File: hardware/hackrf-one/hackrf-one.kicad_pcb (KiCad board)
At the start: 4 copper layers, 120 x 75 mm, 434 parts, among them J10 GND_CLIP, J11 Connector_USB_C_Receptacle_US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, J2 RF-SHIELD-FRAME, J3 RF-SHIELD-COVER, J4 MOUNTING_HOLE, J5 MOUNTING_HOLE, J6 MOUNTING_HOLE, J7 MOUNTING_HOLE, J8 MOUNTING_HOLE, J9 MOUNTING_HOLE, P1 1V8, P13 GPO1, P14 XCVR_CLKOUT, P15 INTR, P16 CLKIN, P17 GPO6, P18 OEB, P19 GPO3, P2 CLKOUT, P20 GPIO, P21 REF_IN, P22 I2S, P23 DBGEN, P24 TRST, P25 LPC_ISP, P26 LPC_JTAG, P27 MIXER_SDATA, P28 SD, P29 CPLD_JTAG, P3 GND, P30 BANK2_AUX, P31 MIXER_SCLK, P32 MIXER_ENX, P33 MIXER_RESETX, P34 MIX_BYPASS, P35 !MIX_BYPASS, P36 VAA, P37 SCL, P38 SDA, P39 SSP1_SCK, P4 ANTENNA, P40 SSP1_MOSI, P41 SSP1_MISO, P43 RX, P44 HP, P45 LP, P46 TX_MIX_BP, P47 RX_MIX_BP, P48 TX_AMP, P49 RX_AMP, P5 LEDS, P50 AMP_BYPASS, P51 !TX_AMP_PWR, P52 !RX_AMP_PWR, P53 CS_XCVR, P54 CS_AD, P55 TXENABLE, P56 RXENABLE, P57 XTAL2, P58 GCK1, P59 GCK2, P6 GPO4, P60 SGPIO_CLK, P61 DA0, P62 DA7, P63 DD0, P64 DD9, P65 DA4, P66 DD5, P67 RSSI, P68 SPIFI_CS, P69 VREGMODE, P7 GPO2, P70 EN_1V8, P72 GP_CLKIN, P73 P1_2, P74 P1_1, P75 GP_CLKIN, P76 GP_CLKIN, P77 GP_CLKIN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

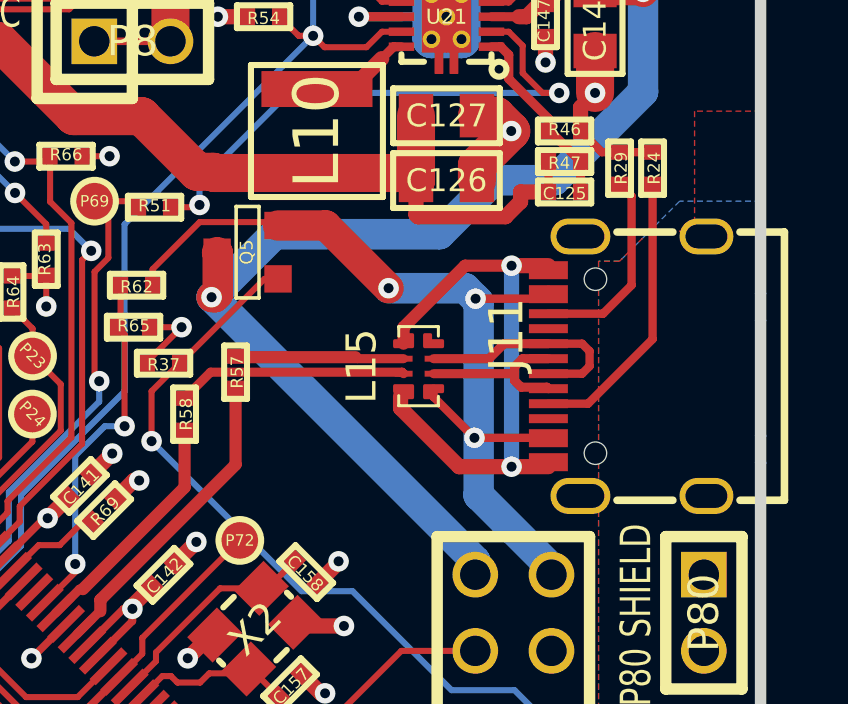
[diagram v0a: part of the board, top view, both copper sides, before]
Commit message: Updated to move USB-C connector to save location as OpenSourceSDRLab's R10C
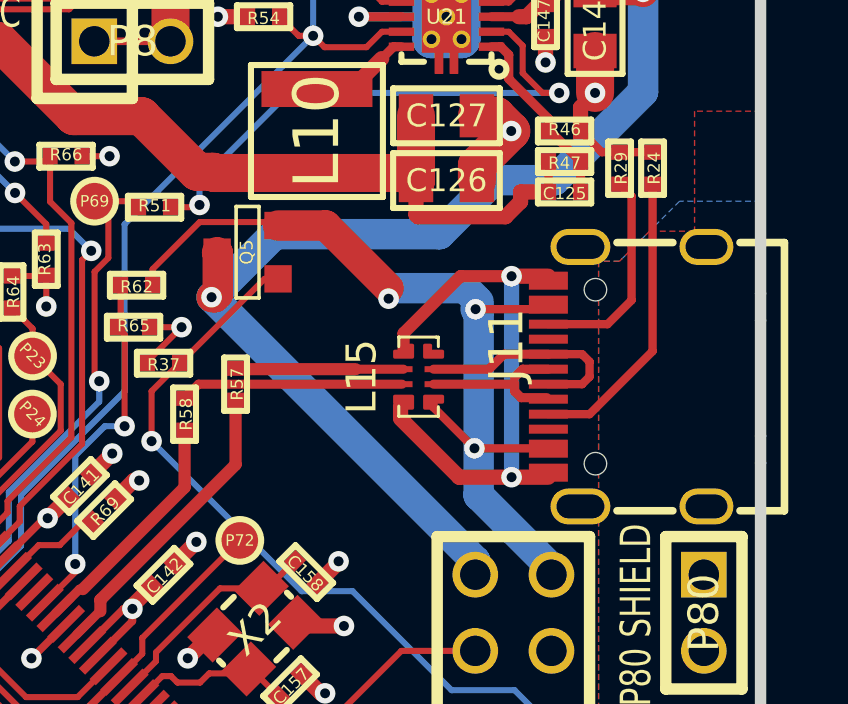
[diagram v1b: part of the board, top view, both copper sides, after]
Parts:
- moved R57 0.40 mm to (151.3, 106.5)
- moved J11 0.35 mm to (164.4, 106.2)
- moved L15 0.35 mm to (157.4, 106.2)
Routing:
- net /mcu/usb/power/VBUS: track 31.8 -> 31.1 mm

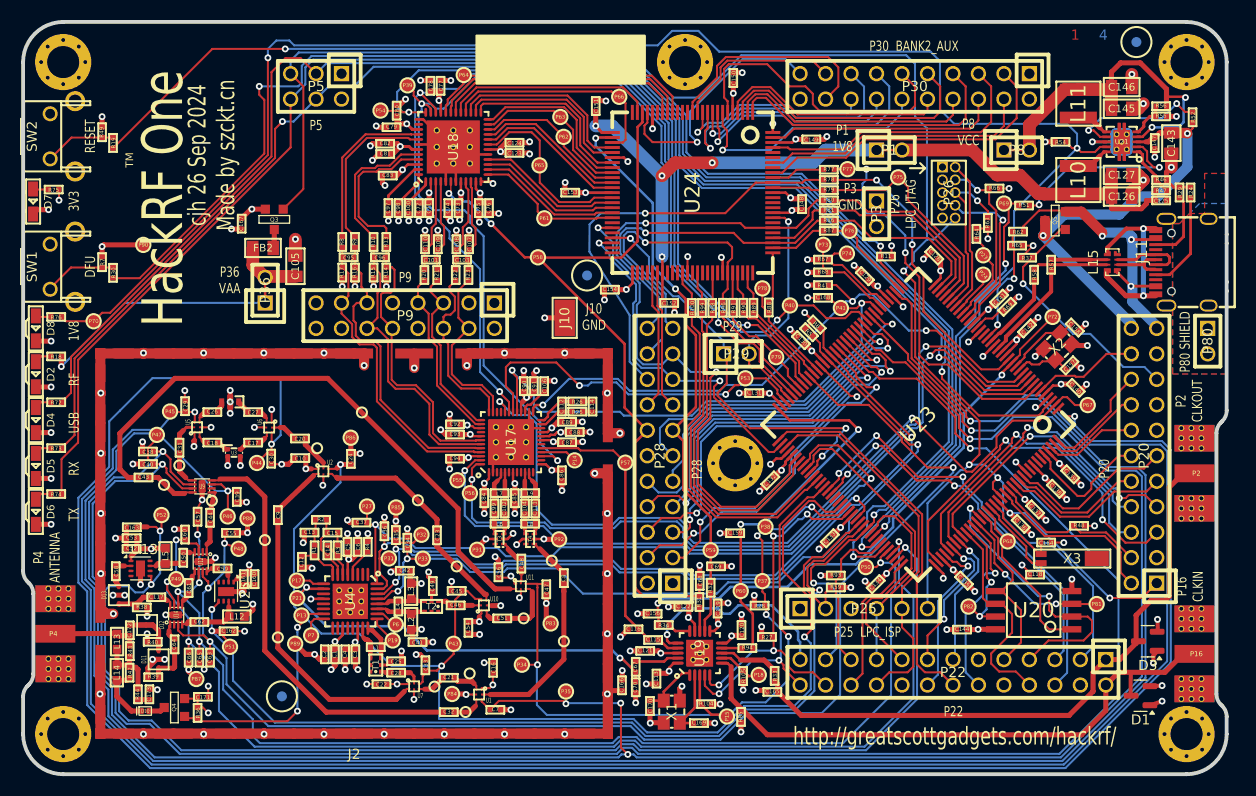
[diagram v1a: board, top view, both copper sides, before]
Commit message: Made design changes to indicate version 15. Correct Q3/4/5 part-no and LPF rotation
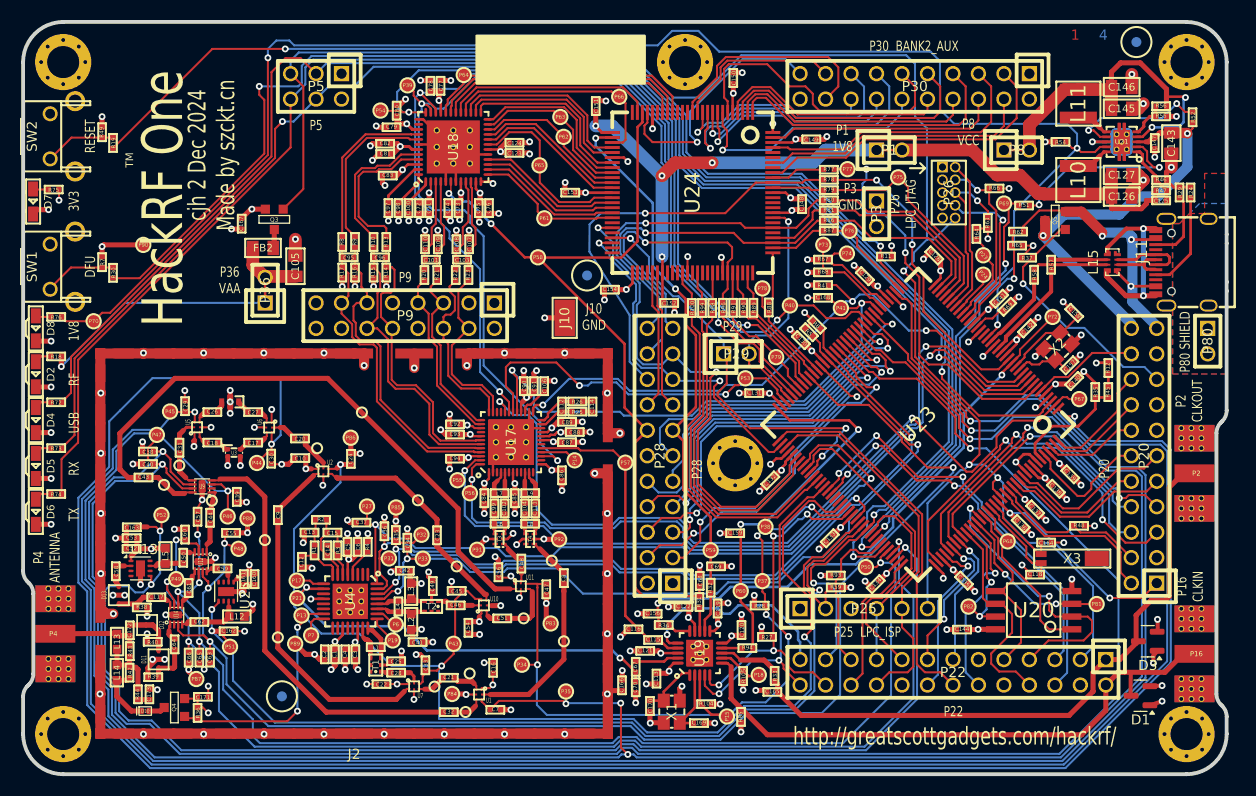
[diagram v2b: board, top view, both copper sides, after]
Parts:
- added R12: 100k, hackrf:GSG-0402, F.Cu at (157.0, 116.8)
- added R35: 220k, hackrf:GSG-0402, F.Cu at (155.7, 119.2)
- added R45: 6.8k, hackrf:GSG-0402, F.Cu at (157.0, 119.2)
- D11, D12, D13: value CLA4611 -> CLA4611-085LF
- Q3: value MOSFET_P -> DMP2305U-7
- Q4, Q5: value MOSFET_P -> BSS84
- moved C158 1.46 mm to (153.6, 111.3), turned to 135 degrees
- moved P67 1.04 mm to (154.1, 119.9)
- moved C140 0.70 mm to (153.6, 118.1), turned to 45 degrees
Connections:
- U23 pad 136: unconnected-(U23-ADC0_7/ADC1_7-Pad136) -> VCC
- U23 pad 138: unconnected-(U23-ADC0_4/ADC1_4-Pad138) -> GND
- U23 pad 139: unconnected-(U23-ADC0_3/ADC1_3-Pad139) -> /mcu/usb/power/ADC0_3
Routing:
- net /mcu/usb/power/ADC0_3: track 0.00 -> 11.6 mm
- net GND: track 605.6 -> 609.8 mm
- net VCC: track 219.1 -> 222.2 mm, vias 46 -> 47
- net Net-(R12-Pad2): track 0.00 -> 1.33 mm
- net RSSI: track 83.3 -> 82.2 mm
- net /mcu/usb/power/XTAL2: track 7.43 -> 8.42 mm
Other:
- board text added: "cjh 2 Dec 2024 Made by szckt.cn"
- board text removed: "cjh 26 Sep 2024 Made by szckt.cn"

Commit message: Added U15 version detection resistors, corrected FETs and U3 rotation
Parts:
- Q3: value DMP2305U-7 -> AO3407A
- Q4, Q5: value BSS84 -> AO3407A
